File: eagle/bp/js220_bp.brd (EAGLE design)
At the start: 95 x 24.7 mm, 9 parts, among them J1 111-0703-001, J2 111-0702-001, J4 111-0702-001, J5 TSM-105-01-S-SV

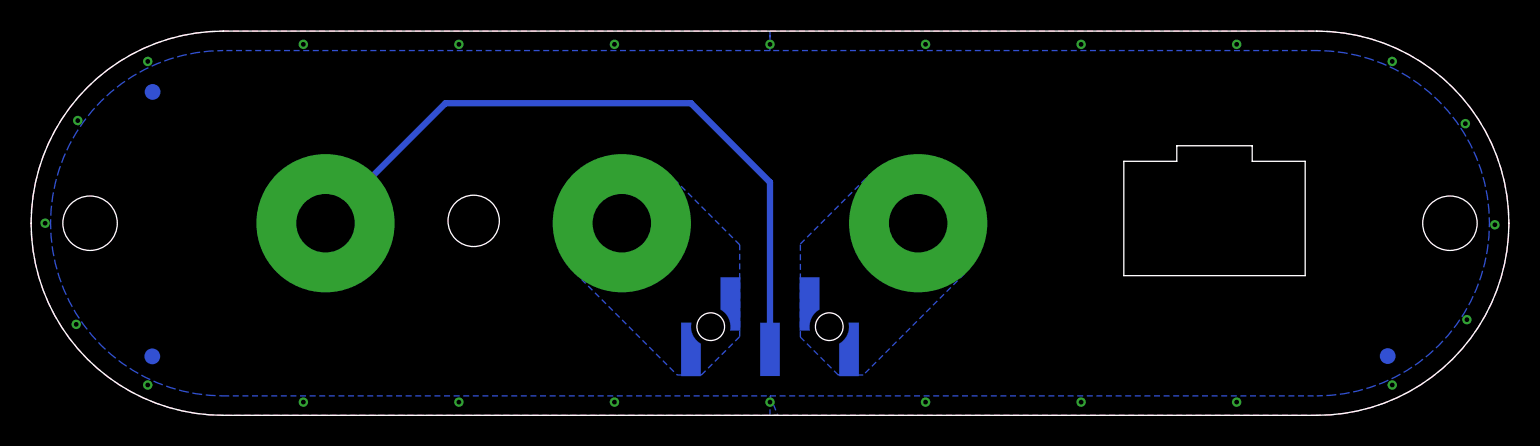
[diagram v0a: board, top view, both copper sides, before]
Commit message: Completed revA for the initial end panels.
* Binding post front panel.
* Back panel.
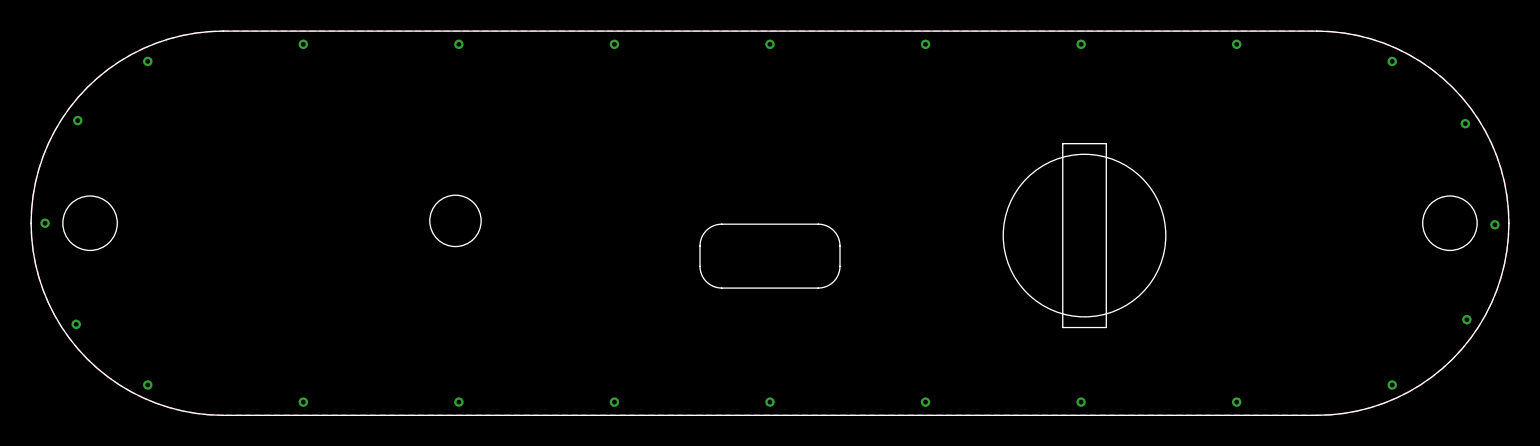
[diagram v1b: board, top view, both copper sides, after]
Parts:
- removed FUD1, FUD2, FUD3: FIDUCIAL_1MM, jetperch:FIDUCIAL_1MM_2MM
- removed J1: 111-0703-001, jetperch:BINDING_POST_6
- removed J2, J4: 111-0702-001, jetperch:BINDING_POST_6
- removed J5: TSM-105-01-S-SV, jetperch:CONN_0.1_5X1_MSA
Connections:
- removed net EXT_IN: J2.1, J5.01, J5.02
- removed net EXT_NEG: J1.1, J5.03
- removed net EXT_OUT: J4.1, J5.04, J5.05
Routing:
- net EXT_NEG: track 44.6 -> 0.00 mm
- removed copper zone on layer 16, net EXT_IN
- removed copper zone on layer 16, net EXT_OUT
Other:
- outline, holes or cut-outs redrawn
- board text added: "Green: Normal operation Green pulse: USB standby Blue slow blink: bootloader Red fast blink: error"
- board text added: "JS220 Back Panel Rev A 2021 Jetperch LLC"
- board text added: "Opto-isolated Trigger with 2.6V to 5.5 V"
- board text added: "To host computer"
- board text added: "Trigger In"
- board text added: "USB"
- board text removed: "Black"
- board text removed: "Current + -"
- board text removed: "Gnd In1 In3 Out1"
- board text removed: "JS220 Binding Post Front Panel Rev A 2021 Jetperch LLC"
- board text removed: "Red"
- board text removed: "Voltage - +"
- board text removed: "Vref In0 In2 Out0"
- board text removed: "Yellow"

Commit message: Updated to rev B.
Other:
- board text added: "JS220 Back Panel Rev B 2022 Jetperch LLC"
- board text added: "Out: 3.3V, 50 Ω In: 3.3V & TTL compatible"
- board text added: "Trigger In/Out"
- board text removed: "JS220 Back Panel Rev A 2021 Jetperch LLC"
- board text removed: "Opto-isolated Trigger with 2.6V to 5.5 V"
- board text removed: "Trigger In"
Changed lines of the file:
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@@
 <drawing>
 <settings>
-<setting alwaysvectorfont="yes"/>
+<setting alwaysvectorfont="no"/>
 <setting verticaltext="up"/>
 </settings>
@@
 <plain>
 <text x="47.5" y="20.2" size="1.27" layer="26" font="vector" ratio="20" rot="MR0" align="center">JS220 Back Panel
-Rev A
-2021 Jetperch LLC</text>
+Rev B
+2022 Jetperch LLC</text>
 <dimension x1="0" y1="12.35" x2="95" y2="12.35" x3="47.5" y3="40.64" textsize="1.778" layer="47" dtype="horizontal"/>
 <dimension x1="12.35" y1="0" x2="12.35" y2="24.7" x3="-6.35" y3="12.35" textsize="1.778" layer="47" dtype="vertical"/>
@@
 <wire x1="66.32" y1="5.645" x2="66.32" y2="17.465" width="0" layer="20"/>
 <text x="47.5" y="20" size="1.5" layer="29" font="vector" ratio="20" align="center">USB</text>
-<text x="67.72" y="20" size="1.5" layer="29" font="vector" ratio="20" align="center">Trigger In</text>
-<text x="67.72" y="2" size="1" layer="29" font="vector" ratio="20" align="bottom-center">Opto-isolated
-Trigger with 2.6V to 5.5 V</text>
+<text x="67.72" y="20" size="1.5" layer="29" font="vector" ratio="20" align="center">Trigger
+In/Out</text>
+<text x="67.72" y="2" size="1" layer="29" font="vector" ratio="20" align="bottom-center">Out: 3.3V, 50 Ω
+In: 3.3V &amp; TTL compatible</text>
 <text x="47.5" y="2" size="1" layer="29" font="vector" ratio="20" align="bottom-center">To host computer
 </text>
